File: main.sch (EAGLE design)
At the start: 87 parts, among them Q1 5.8A/30V/35mΩ, Q2 5.8A/30V/35mΩ, Q3 2.5A/30V/105mΩ, U1 BQ24133_RGY_24, U2 SN65HVD32_D_8

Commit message: First Layout and Schematic
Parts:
- removed 103AT-THERMISTOR: 10k, pinhead:PINHD-1X2
- removed BATT, VCHG: (no value), pinhead:PINHD-1X2
- removed C10, C11, C22, C25: 1u, resistor:C-USC0603
- removed C12: 2.2u, resistor:C-USC0603
- removed C13, C14, C16, C18, C21, C5, C8: 100n, resistor:C-USC0603
- removed C15, C19: 10u, resistor:C-USC0603
- removed C17: 47n, resistor:C-USC0603
- removed C4: 6.8n, resistor:C-USC0603
- removed CHG-STAT: 2V @ 20mA, adafruit:LEDCHIPLED_0603
- removed D1: BAS70-05, diode:BAS70-05
- removed GND-JMP, R23: 0, resistor:R-US_R0603
- removed IMU: BNO055, BNO055:BNO055
- removed L2: 6.8u, ipc-7351-inductor:INDUCTOR_1008
- removed Q1, Q2: 5.8A/30V/35mΩ, SparkFun-DiscreteSemi:MOSFET-NCH-AO3404A
- removed Q3: 2.5A/30V/105mΩ, SparkFun-DiscreteSemi:MOSFET_PCH-DMG2307L
- removed R1, R22: 100k, resistor:R-US_R0603
- removed R10: 2, resistor:R-US_R0603
- removed R11, R12: 4.02k, resistor:R-US_R0603
- removed R13: 20m, resistor:R-US_R0603
- removed R2: 3.8k, resistor:R-US_R0603
- removed R26, R29, R38, R39: 1k, resistor:R-US_R0603
- removed R27: 10m, resistor:R-US_R0603
- removed R33: 13.8k, resistor:R-US_R0603
- removed R36: 5.23k, resistor:R-US_R0603
- removed R37: 30.1k, resistor:R-US_R0603
- removed R4, R6: 10k, resistor:R-US_R0603
- removed R42: 64.9, resistor:R-US_R0603
- removed R7: 10, resistor:R-US_R0603
- removed R8: 1M, resistor:R-US_R0603
- removed R9: 113k, resistor:R-US_R0603
- removed U1: BQ24133_RGY_24, BQ24133-UPDATED:BQ24133_RGY_24
- added VIN: (no value), pinhead:PINHD-1X2
- GPIO: device pinhead:PINHD-1X10 -> pinhead:PINHD-1X8
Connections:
- removed net *BATDRV: R26.2, U1.*BATDRV
- removed net AGND: 103AT-THERMISTOR.2, C10.2, C11.2, C14.2, C18.2, C21.2, C25.2, GND-JMP.2, R2.1, R33.1, R37.2, R9.1, U1.EPAD, VCHG.2
- removed net BATT: BATT.1, C16.1, C19.1, C21.1, D1.A2, Q3.D, R27.1, U1.SRN
- removed net GPIO10: GPIO.10
- removed net GPIO9: GPIO.9
- removed net IMU_INT: IMU.INT
- removed net N$15: C12.1, R10.1
- removed net N$16: Q1.S, Q2.S, R11.2
- removed net N$17: Q1.G, Q2.G, R12.2
- removed net N$18: IMU.NBOOT_LOAD_PIN, R6.2
- removed net N$19: SD.CD/DAT3
- removed net N$21: C10.1, R7.2, U1.AVCC
- removed net N$23: CHG-STAT.A, R42.2
- removed net NRESET: IMU.NRESET, R4.2
- removed net PA16_SER1_I2C_SDA: IMU.COM0, MCU.PA16(I2C/SER1:0+), R38.2
- removed net PA17_SER1_I2C_SCL: IMU.COM1, MCU.PA17(I2C/SER1:1+), R39.2
- removed net PC_ACDRV: R12.1, U1.ACDRV
- removed net PC_ACN: C13.2, C14.1, R13.1, R23.2, U1.ACN
- removed net PC_ACP: C13.1, Q2.D, R13.2, U1.ACP
- removed net PC_ACSET: R1.1, R33.2, U1.ACSET
- removed net PC_BTST: C17.2, U1.BTST
- removed net PC_CELL: R29.2, U1.CELL
- removed net PC_CMSRC: R11.1, U1.CMSRC
- removed net PC_ISET: R2.2, R22.1, U1.ISET
- removed net PC_OVPSET: R8.1, R9.2, U1.OVPSET
- removed net PC_PVCC: C15.1, Q3.S, R23.1, S2.P, U1.PVCC, U1.PVCC_2
- removed net PC_REGN: C22.1, U1.REGN
- removed net PC_SRP: C16.2, C18.1, L2.2, R27.2, U1.SRP
- removed net PC_STAT: CHG-STAT.C, U1.STAT
- removed net PC_SW: C17.1, L2.1, U1.SW, U1.SW_2
- removed net PC_TS: 103AT-THERMISTOR.1, R36.2, R37.1, U1.TS
- removed net PC_TTC: C25.1, U1.TTC
- removed net PC_VREF: C11.1, R1.2, R22.2, R29.1, R36.1, R42.1, U1.VREF
- removed net VIN: D1.A1, Q1.D, R10.2, R8.2, VCHG.1
- net 3.3V: no longer C4.1, C5.1, IMU.VDD, IMU.VDDIO, R38.1, R39.1, R4.1, R6.1
- net AIN0: now also MCU.PA07(AIN7/SER0:3/TC1:1)
- net AIN1: now also MCU.PA11(AIN19/SER0:3+)
- net AIN2: now also MCU.PA10(AIN18/SER0:2+)
- net AIN3: now also MCU.PA09(I2C/AIN17/SER0:1+)
- net AIN4: now also MCU.PA08(I2C/AIN16/SER0:0+)
- net GND: now also VIN.1; no longer BATT.2, C12.2, C15.2, C19.2, C22.2, C4.2, C5.2, C8.2, GND-JMP.1, IMU.COM2, IMU.COM3, IMU.GND, IMU.GNDIO, IMU.PIN10, IMU.PIN15, IMU.PIN16, IMU.PS0, IMU.PS1, U1.PGND, U1.PGND_2
- net GPIO1: now also MCU.PA23(I2C/SER3:0+)
- net GPIO2: now also MCU.PA22(I2C/SER3:0+)
- net GPIO3: now also MCU.PA21(SER5:3+)
- net GPIO4: now also MCU.PA20(SER5:2+)
- net GPIO5: now also MCU.PA19(SER1:3+)
- net GPIO6: now also MCU.PA18(SER1:2+)
- net GPIO7: now also MCU.PA17(I2C/SER1:1+)
- net GPIO8: now also MCU.PA16(I2C/SER1:0+)
- net N$10: now also MCU.PA25(SER3:3+), R41.1; no longer Q3.G, R26.1
- net N$14: now also MCU.PA24(SER3:2+), R28.1; no longer D1.C, R7.1
- net N$9: now also S2.P, VIN.2; no longer C8.1, IMU.CAP
- net SD_CS: now also MCU.PA04(AIN4/REFB/SER0:0/TC0:0), SD.CD/DAT3; no longer MCU.PA00(XIN32/SER1:0/TC2:0)
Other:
- note removed: "* MEANS UNFINISHED"
- note removed: "CAUTION: NEED to know source(ducers) impedance before picking voltage divider resistor values. Also the samd21 adc has a maximum source impedance of 3.5kohms."
- note removed: "NOT SURE IF INTERNAL PULLUP FOR RESET"
- note removed: "POWER SCHEMS ON PG2"

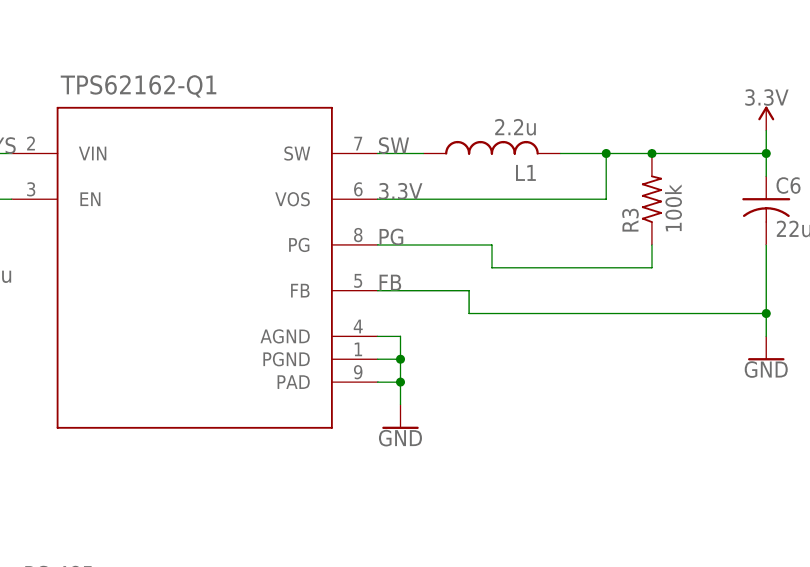
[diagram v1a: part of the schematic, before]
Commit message: Added gnd pour
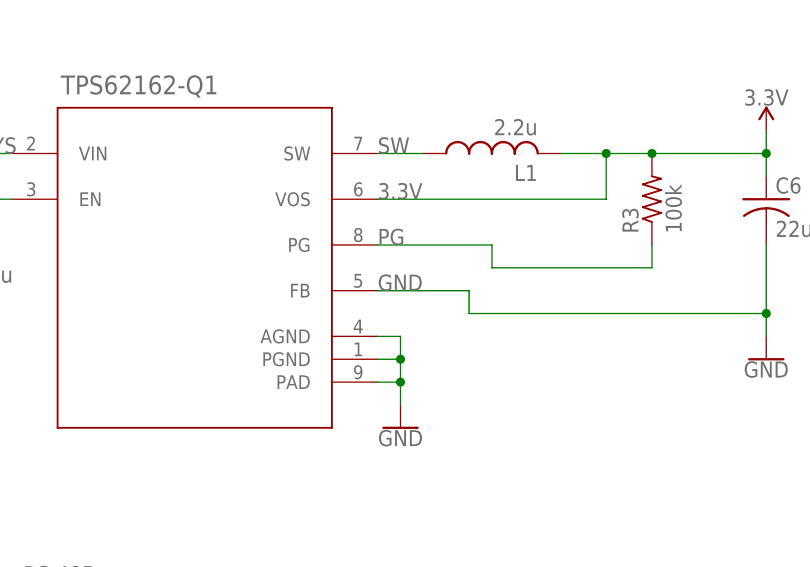
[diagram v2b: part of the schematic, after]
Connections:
- removed net FB: C6.2, TPS62162-Q1.FB
- net GND: now also C6.2, TPS62162-Q1.FB
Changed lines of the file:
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@@
 <wire x1="477.52" y1="134.62" x2="474.98" y2="134.62" width="0.1524" layer="91"/>
+</segment>
+<segment>
+<pinref part="C6" gate="G$1" pin="2"/>
+<wire x1="601.98" y1="121.92" x2="601.98" y2="129.54" width="0.1524" layer="91"/>
+<wire x1="601.98" y1="121.92" x2="601.98" y2="119.38" width="0.1524" layer="91"/>
+<junction x="601.98" y="121.92"/>
+<pinref part="GND8" gate="1" pin="GND"/>
+<wire x1="601.98" y1="121.92" x2="568.96" y2="121.92" width="0.1524" layer="91"/>
+<pinref part="TPS62162-Q1" gate="A" pin="FB"/>
+<wire x1="558.8" y1="124.46" x2="568.96" y2="124.46" width="0.1524" layer="91"/>
+<wire x1="568.96" y1="121.92" x2="568.96" y2="124.46" width="0.1524" layer="91"/>
+<label x="558.8" y="124.46" size="1.778" layer="95"/>
 </segment>
 </net>
@@
 </segment>
 </net>
-<net name="FB" class="0">
-<segment>
-<pinref part="C6" gate="G$1" pin="2"/>
-<wire x1="601.98" y1="121.92" x2="601.98" y2="129.54" width="0.1524" layer="91"/>
-<wire x1="601.98" y1="121.92" x2="601.98" y2="119.38" width="0.1524" layer="91"/>
-<junction x="601.98" y="121.92"/>
-<pinref part="GND8" gate="1" pin="GND"/>
-<wire x1="601.98" y1="121.92" x2="568.96" y2="121.92" width="0.1524" layer="91"/>
-<pinref part="TPS62162-Q1" gate="A" pin="FB"/>
-<wire x1="558.8" y1="124.46" x2="568.96" y2="124.46" width="0.1524" layer="91"/>
-<wire x1="568.96" y1="121.92" x2="568.96" y2="124.46" width="0.1524" layer="91"/>
-<label x="558.8" y="124.46" size="1.778" layer="95"/>
-</segment>
-</net>

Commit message: Added IMU
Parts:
- added C4: 6.8n, resistor:C-USC0603
- added C5, C8: 100n, resistor:C-USC0603
- added IMU: BNO055, BNO055:BNO055
- added R38, R39: 1k, resistor:R-US_R0603
- added R4, R6: 10k, resistor:R-US_R0603
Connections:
- new net IMU_INT: IMU.INT
- new net N$15: C8.1, IMU.CAP
- new net N$18: IMU.NBOOT_LOAD_PIN, R6.2
- new net NRESET: IMU.NRESET, R4.2
- new net PA16_SER1_I2C_SDA: IMU.COM0, MCU.PA16(I2C/SER1:0+), R38.2
- new net PA17_SER1_I2C_SCL: IMU.COM1, MCU.PA17(I2C/SER1:1+), R39.2
- net 3.3V: now also C4.1, C5.1, IMU.VDD, IMU.VDDIO, R38.1, R39.1, R4.1, R6.1
- net GND: now also C4.2, C5.2, C8.2, IMU.COM2, IMU.COM3, IMU.GND, IMU.GNDIO, IMU.PIN10, IMU.PIN15, IMU.PIN16, IMU.PS0, IMU.PS1
- net GPIO7: no longer MCU.PA17(I2C/SER1:1+)
- net GPIO8: no longer MCU.PA16(I2C/SER1:0+)
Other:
- note added: "* MEANS UNFINISHED"

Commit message: Schematic and Layout Optimizations
Reconfigured a couple serial pins to make trace routing easier. Placed all compnents, just need to route and label.
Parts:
- added R1: 10k, resistor:R-US_R0603
- renumbered GND to VDD
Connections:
- removed net N$10: MCU.PA25(SER3:3+), R41.1
- removed net PB08D_SER4_P0: MCU.PB08(AIN2/SER4:0/TC4:0), SD.CMD
- removed net PB09D_SER4_P1: MCU.PB09(AIN3/SER4:1/TC4:1), SD.CLK
- removed net PB11D_SER4_P3: MCU.PB11(SER4:3+), SD.DAT0
- new net N$16: MCU.PA00(XIN32/SER1:0/TC2:0), R41.1
- new net SER0_P0_DI: MCU.PA08(I2C/AIN16/SER0:0+), SD.DAT0
- new net SER0_P1_CLK: MCU.PA09(I2C/AIN17/SER0:1+), SD.CLK
- new net SER0_P3_DO: MCU.PA11(AIN19/SER0:3+), SD.CMD
- net 3.3V: now also R1.1, VDD.1
- net AIN0: now also MCU.PA06(AIN6/SER0:2/TC1:0); no longer MCU.PA07(AIN7/SER0:3/TC1:1)
- net AIN1: now also MCU.PA05(AIN5/SER0:1/TC0:1); no longer MCU.PA11(AIN19/SER0:3+)
- net AIN2: now also MCU.PA04(AIN4/REFB/SER0:0/TC0:0); no longer MCU.PA10(AIN18/SER0:2+)
- net AIN3: now also MCU.PB09(AIN3/SER4:1/TC4:1); no longer MCU.PA09(I2C/AIN17/SER0:1+)
- net AIN4: now also MCU.PB08(AIN2/SER4:0/TC4:0); no longer MCU.PA08(I2C/AIN16/SER0:0+)
- net GND: no longer VDD.1
- net GPIO1: now also MCU.PA27; no longer MCU.PA23(I2C/SER3:0+)
- net GPIO2: now also MCU.PB23(SER5:3+); no longer MCU.PA22(I2C/SER3:0+)
- net GPIO3: now also MCU.PB22(SER5:2+); no longer MCU.PA21(SER5:3+)
- net GPIO4: now also MCU.PA22(I2C/SER3:0+); no longer MCU.PA20(SER5:2+)
- net GPIO5: now also MCU.PA21(SER5:3+); no longer MCU.PA19(SER1:3+)
- net GPIO6: now also MCU.PA20(SER5:2+); no longer MCU.PA18(SER1:2+)
- net GPIO7: now also MCU.PA19(SER1:3+)
- net GPIO8: now also MCU.PA18(SER1:2+)
- net MCU_RX: now also MCU.PA23(I2C/SER3:0+); no longer MCU.PB23(SER5:3+)
- net MCU_TX: now also MCU.PA24(SER3:2+); no longer MCU.PB22(SER5:2+)
- net N$14: now also MCU.PA01(XOUT32/SER1:1/TC2:1); no longer MCU.PA24(SER3:2+)
- net SD_CD: now also MCU.PA07(AIN7/SER0:3/TC1:1); no longer MCU.PA03(AIN1/REFA)
- net SD_CS: now also MCU.PA12(I2C/SER2:0+), R1.2; no longer MCU.PA04(AIN4/REFB/SER0:0/TC0:0)
- net VSYS: now also S2.S; no longer S2.O
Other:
- note added: "DIPO: 0x0"
- note added: "DOPO: 0x2"
- moved on the sheet: LED0, LED1, R28, R41, S2, VIN

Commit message: Routed everything
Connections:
- net SD_CS: now also MCU.PB10(SER4:2+); no longer MCU.PA12(I2C/SER2:0+)
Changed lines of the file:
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@@
 <?xml version="1.0" encoding="utf-8"?>
 <!DOCTYPE eagle SYSTEM "eagle.dtd">
-<eagle version="8.6.3">
+<eagle version="8.6.0">
 <drawing>
 <settings>
@@
 <grid distance="0.1" unitdist="inch" unit="inch" style="lines" multiple="1" display="no" altdistance="0.01" altunitdist="inch" altunit="inch"/>
 <layers>
-<layer number="1" name="Top" color="4" fill="1" visible="no" active="no"/>
-<layer number="2" name="Route2" color="1" fill="3" visible="no" active="no"/>
-<layer number="3" name="Route3" color="4" fill="3" visible="no" active="no"/>
-<layer number="4" name="Route4" color="1" fill="4" visible="no" active="no"/>
-<layer number="5" name="Route5" color="4" fill="4" visible="no" active="no"/>
-<layer number="6" name="Route6" color="1" fill="8" visible="no" active="no"/>
-<layer number="7" name="Route7" color="4" fill="8" visible="no" active="no"/>
-<layer number="8" name="Route8" color="1" fill="2" visible="no" active="no"/>
-<layer number="9" name="Route9" color="4" fill="2" visible="no" active="no"/>
-<layer number="10" name="Route10" color="1" fill="7" visible="no" active="no"/>
-<layer number="11" name="Route11" color="4" fill="7" visible="no" active="no"/>
-<layer number="12" name="Route12" color="1" fill="5" visible="no" active="no"/>
-<layer number="13" name="Route13" color="4" fill="5" visible="no" active="no"/>
-<layer number="14" name="Route14" color="1" fill="6" visible="no" active="no"/>
-<layer number="15" name="Route15" color="4" fill="6" visible="no" active="no"/>
-<layer number="16" name="Bottom" color="1" fill="1" visible="no" active="no"/>
-<layer number="17" name="Pads" color="2" fill="1" visible="no" active="no"/>
-<layer number="18" name="Vias" color="2" fill="1" visible="no" active="no"/>
-<layer number="19" name="Unrouted" color="6" fill="1" visible="no" active="no"/>
-<layer number="20" name="Dimension" color="24" fill="1" visible="no" active="no"/>
-<layer number="21" name="tPlace" color="7" fill="1" visible="no" active="no"/>
-<layer number="22" name="bPlace" color="7" fill="1" visible="no" active="no"/>
-<layer number="23" name="tOrigins" color="15" fill="1" visible="no" active="no"/>
-<layer number="24" name="bOrigins" color="15" fill="1" visible="no" active="no"/>
-<layer number="25" name="tNames" color="7" fill="1" visible="no" active="no"/>
-<layer number="26" name="bNames" color="7" fill="1" visible="no" active="no"/>
-<layer number="27" name="tValues" color="7" fill="1" visible="no" active="no"/>
-<layer number="28" name="bValues" color="7" fill="1" visible="no" active="no"/>
+<layer number="1" name="Top" color="4" fill="1" visible="yes" active="no"/>
+<layer number="2" name="Route2" color="1" fill="3" visible="yes" active="no"/>
+<layer number="3" name="Route3" color="4" fill="3" visible="yes" active="no"/>
+<layer number="4" name="Route4" color="1" fill="4" visible="yes" active="no"/>
+<layer number="5" name="Route5" color="4" fill="4" visible="yes" active="no"/>
+<layer number="6" name="Route6" color="1" fill="8" visible="yes" active="no"/>
+<layer number="7" name="Route7" color="4" fill="8" visible="yes" active="no"/>
+<layer number="8" name="Route8" color="1" fill="2" visible="yes" active="no"/>
+<layer number="9" name="Route9" color="4" fill="2" visible="yes" active="no"/>
+<layer number="10" name="Route10" color="1" fill="7" visible="yes" active="no"/>
+<layer number="11" name="Route11" color="4" fill="7" visible="yes" active="no"/>
+<layer number="12" name="Route12" color="1" fill="5" visible="yes" active="no"/>
+<layer number="13" name="Route13" color="4" fill="5" visible="yes" active="no"/>
+<layer number="14" name="Route14" color="1" fill="6" visible="yes" active="no"/>
+<layer number="15" name="Route15" color="4" fill="6" visible="yes" active="no"/>
+<layer number="16" name="Bottom" color="1" fill="1" visible="yes" active="no"/>
+<layer number="17" name="Pads" color="2" fill="1" visible="yes" active="no"/>
+<layer number="18" name="Vias" color="2" fill="1" visible="yes" active="no"/>
+<layer number="19" name="Unrouted" color="6" fill="1" visible="yes" active="no"/>
+<layer number="20" name="Dimension" color="24" fill="1" visible="yes" active="no"/>
+<layer number="21" name="tPlace" color="7" fill="1" visible="yes" active="no"/>
+<layer number="22" name="bPlace" color="7" fill="1" visible="yes" active="no"/>
+<layer number="23" name="tOrigins" color="15" fill="1" visible="yes" active="no"/>
+<layer number="24" name="bOrigins" color="15" fill="1" visible="yes" active="no"/>
+<layer number="25" name="tNames" color="7" fill="1" visible="yes" active="no"/>
+<layer number="26" name="bNames" color="7" fill="1" visible="yes" active="no"/>
+<layer number="27" name="tValues" color="7" fill="1" visible="yes" active="no"/>
+<layer number="28" name="bValues" color="7" fill="1" visible="yes" active="no"/>
 <layer number="29" name="tStop" color="7" fill="3" visible="no" active="no"/>
 <layer number="30" name="bStop" color="7" fill="6" visible="no" active="no"/>
@@
 <layer number="35" name="tGlue" color="7" fill="4" visible="no" active="no"/>
 <layer number="36" name="bGlue" color="7" fill="5" visible="no" active="no"/>
-<layer number="37" name="tTest" color="7" fill="1" visible="no" active="no"/>
-<layer number="38" name="bTest" color="7" fill="1" visible="no" active="no"/>
+<layer number="37" name="tTest" color="7" fill="1" visible="yes" active="no"/>
+<layer number="38" name="bTest" color="7" fill="1" visible="yes" active="no"/>
 <layer number="39" name="tKeepout" color="4" fill="11" visible="no" active="no"/>
 <layer number="40" name="bKeepout" color="1" fill="11" visible="no" active="no"/>
@@
 <layer number="44" name="Drills" color="7" fill="1" visible="no" active="no"/>
 <layer number="45" name="Holes" color="7" fill="1" visible="no" active="no"/>
-<layer number="46" name="Milling" color="3" fill="1" visible="no" active="no"/>
-<layer number="47" name="Measures" color="7" fill="1" visible="no" active="no"/>
-<layer number="48" name="Document" color="7" fill="1" visible="no" active="no"/>
-<layer number="49" name="Reference" color="7" fill="1" visible="no" active="no"/>
-<layer number="50" name="dxf" color="12" fill="1" visible="no" active="no"/>
-<layer number="51" name="tDocu" color="7" fill="1" visible="no" active="no"/>
-<layer number="52" name="bDocu" color="7" fill="1" visible="no" active="no"/>
-<layer number="53" name="tGND_GNDA" color="7" fill="1" visible="no" active="no"/>
-<layer number="54" name="bGND_GNDA" color="7" fill="1" visible="no" active="no"/>
-<layer number="56" name="wert" color="7" fill="1" visible="no" active="no"/>
-<layer number="57" name="tCAD" color="7" fill="1" visible="no" active="no"/>
-<layer number="59" name="tCarbon" color="7" fill="1" visible="no" active="no"/>
-<layer number="60" name="bCarbon" color="7" fill="1" visible="no" active="no"/>
+<layer number="46" name="Milling" color="3" fill="1" visible="yes" active="no"/>
+<layer number="47" name="Measures" color="7" fill="1" visible="yes" active="no"/>
+<layer number="48" name="Document" color="7" fill="1" visible="yes" active="no"/>
+<layer number="49" name="Reference" color="7" fill="1" visible="yes" active="no"/>
+<layer number="50" name="dxf" color="12" fill="1" visible="yes" active="no"/>
+<layer number="51" name="tDocu" color="7" fill="1" visible="yes" active="no"/>
+<layer number="52" name="bDocu" color="7" fill="1" visible="yes" active="no"/>
+<layer number="53" name="tGND_GNDA" color="7" fill="1" visible="yes" active="no"/>
+<layer number="54" name="bGND_GNDA" color="7" fill="1" visible="yes" active="no"/>
+<layer number="56" name="wert" color="7" fill="1" visible="yes" active="no"/>
+<layer number="57" name="tCAD" color="7" fill="1" visible="yes" active="no"/>
+<layer number="59" name="tCarbon" color="7" fill="1" visible="yes" active="no"/>
+<layer number="60" name="bCarbon" color="7" fill="1" visible="yes" active="no"/>
 <layer number="88" name="SimResults" color="9" fill="1" visible="yes" active="yes"/>
 <layer number="89" name="SimProbes" color="9" fill="1" visible="yes" active="yes"/>
@@
 </segment>
 <segment>
-<pinref part="MCU" gate="G$1" pin="PA12(I2C/SER2:0+)"/>
-<wire x1="203.2" y1="114.3" x2="223.52" y2="114.3" width="0.1524" layer="91"/>
-</segment>
-</net>
+<pinref part="MCU" gate="G$1" pin="PB10(SER4:2+)"/>
+<wire x1="203.2" y1="66.04" x2="220.98" y2="66.04" width="0.1524" layer="91"/>
+<label x="205.74" y="66.04" size="1.778" layer="95"/>
+</segment>
+</net>

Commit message: Small tweaks before labels
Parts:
- added FUNC: (no value), SparkFun-Switches:SWITCH-SPDT-SMD-AYZ0202
- added R2: 10k, resistor:R-US_R0603
- renumbered S2 to PWR
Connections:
- net 3.3V: now also R2.1
- net GND: now also FUNC.S
- net GPIO8: now also FUNC.P, R2.2
